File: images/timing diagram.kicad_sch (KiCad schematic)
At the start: 0 parts

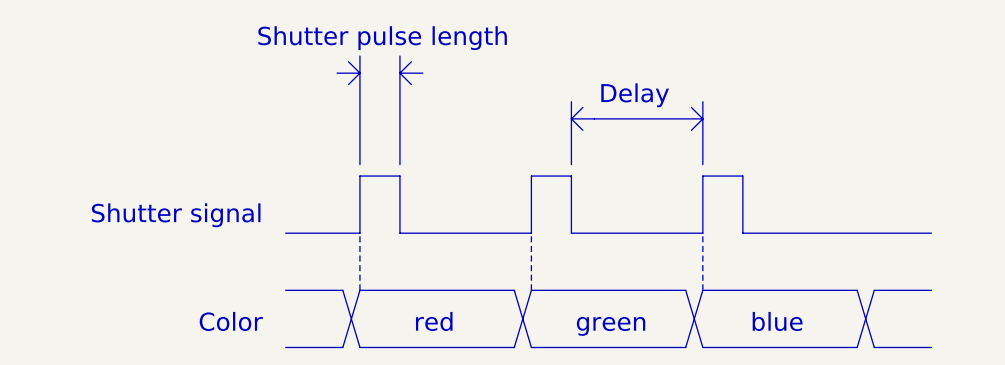
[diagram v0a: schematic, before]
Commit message: add pre-shutter delay and keep light on option to web app
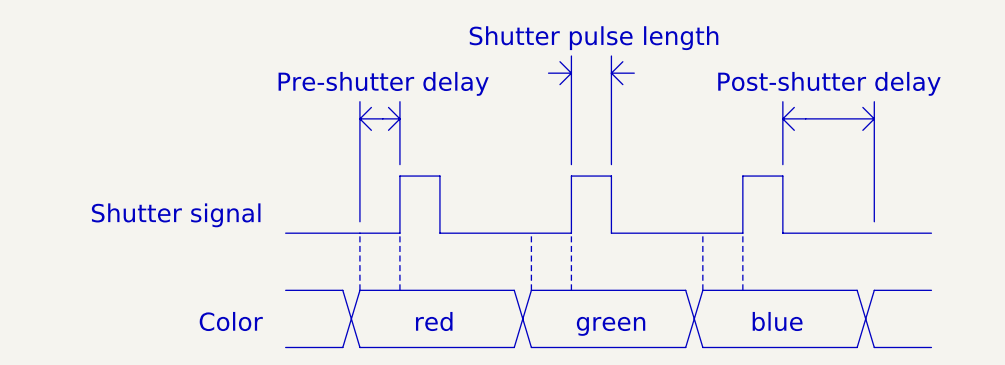
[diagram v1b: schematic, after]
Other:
- note added: "Post-shutter delay"
- note added: "Pre-shutter delay"
- note removed: "Delay"
